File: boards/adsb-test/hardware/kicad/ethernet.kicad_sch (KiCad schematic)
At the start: 0 parts

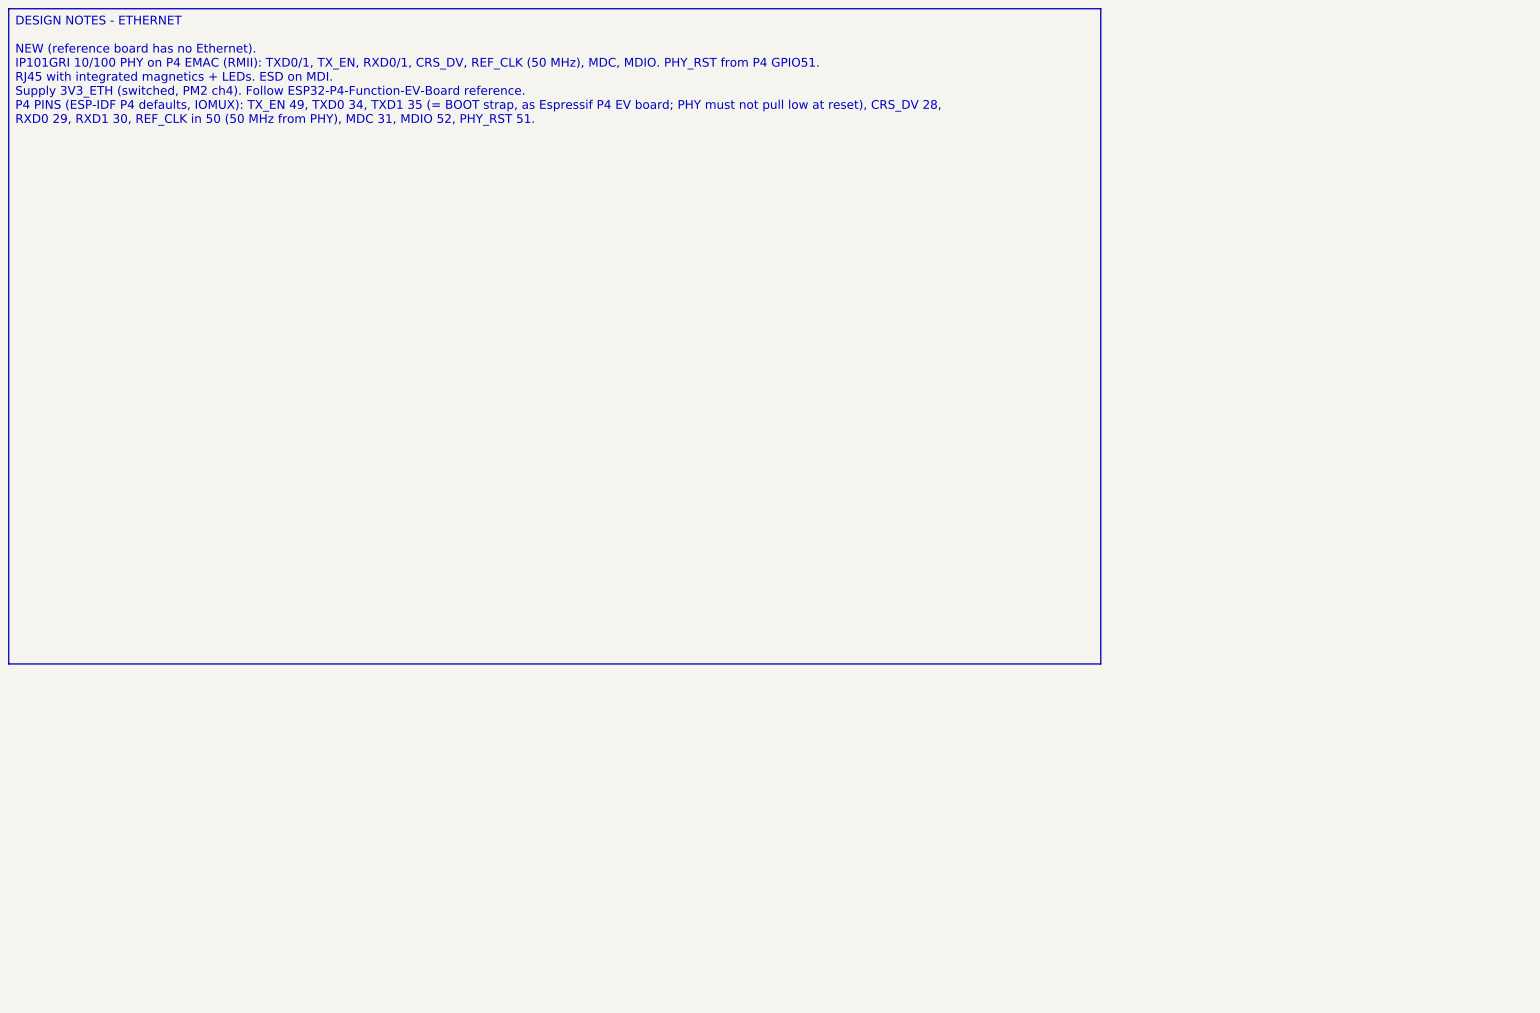
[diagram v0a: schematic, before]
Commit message: Release v0.22.0: all ADSB_Test schematic sheets generated (ERC clean)
Co-Authored-By: Claude Opus 5.5 <noreply@anthropic.com>
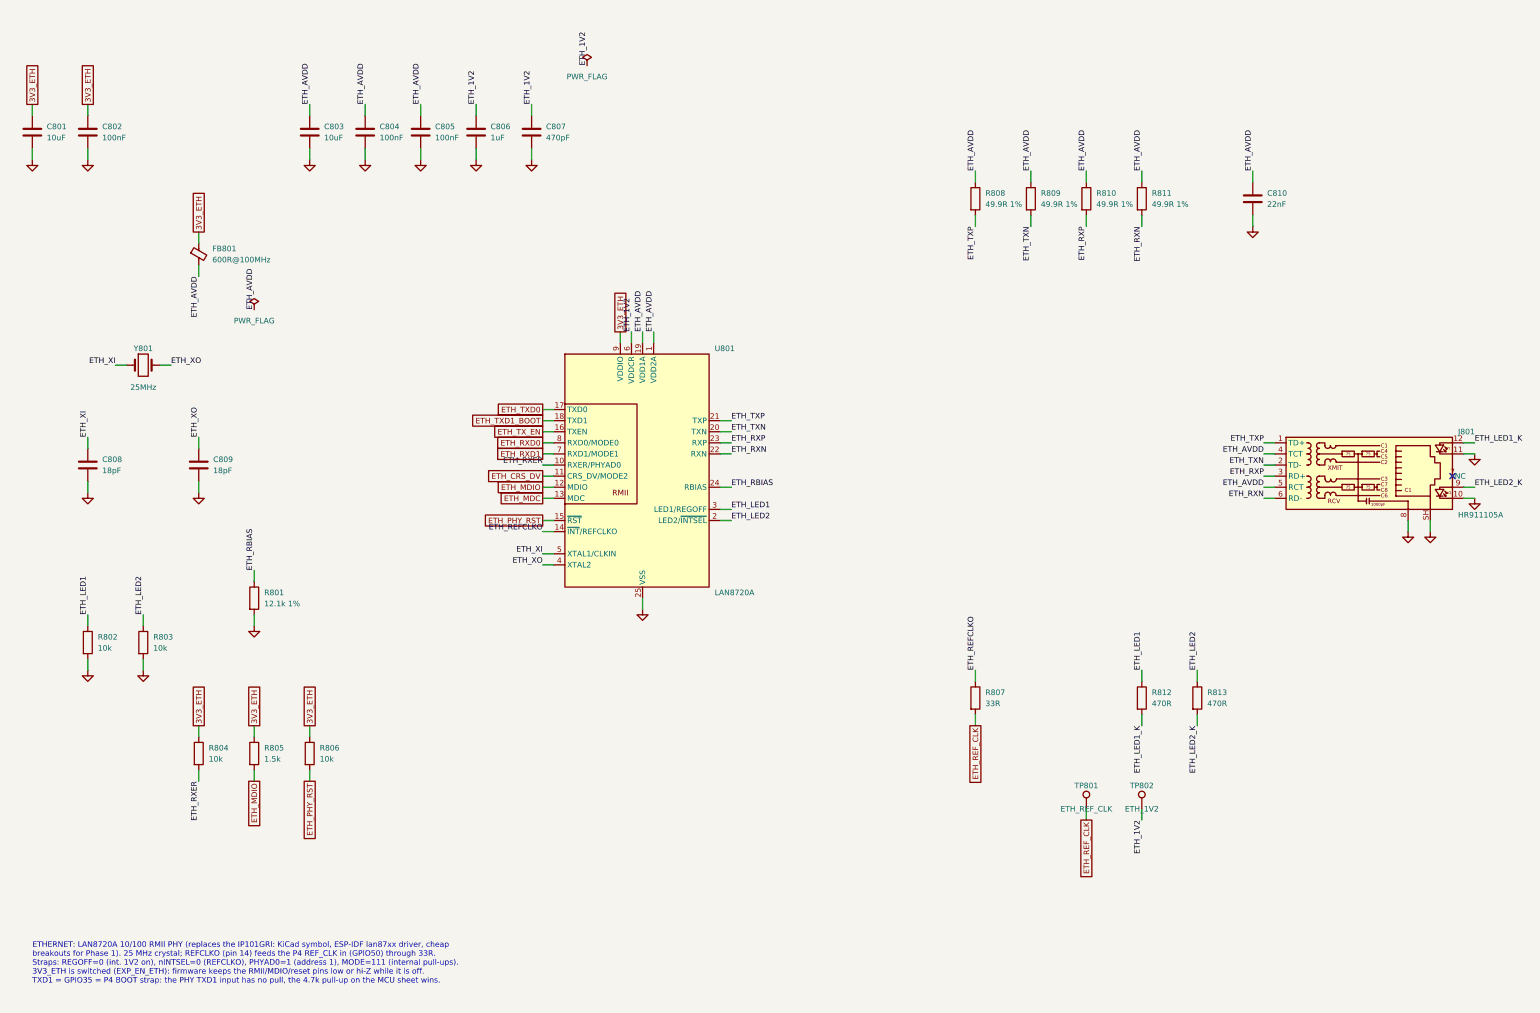
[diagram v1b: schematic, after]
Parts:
- added C801, C803: 10uF, Capacitor_SMD:C_1206_3216Metric_Pad1.33x1.80mm_HandSolder, symbol Device:C
- added C802, C804, C805: 100nF, Capacitor_SMD:C_0805_2012Metric_Pad1.18x1.45mm_HandSolder, symbol Device:C
- added C806: 1uF, Capacitor_SMD:C_0805_2012Metric_Pad1.18x1.45mm_HandSolder, symbol Device:C
- added C807: 470pF, Capacitor_SMD:C_0805_2012Metric_Pad1.18x1.45mm_HandSolder, symbol Device:C
- added C808, C809: 18pF, Capacitor_SMD:C_0805_2012Metric_Pad1.18x1.45mm_HandSolder, symbol Device:C
- added C810: 22nF, Capacitor_SMD:C_0805_2012Metric_Pad1.18x1.45mm_HandSolder, symbol Device:C
- added FB801: 600R@100MHz, Inductor_SMD:L_0805_2012Metric_Pad1.05x1.20mm_HandSolder, symbol Device:FerriteBead_Small
- added J801: HR911105A, Connector_RJ:RJ45_Hanrun_HR911105A_Horizontal, symbol Connector:RJ45_Hanrun_HR911105A_Horizontal
- added R801: 12.1k 1%, Resistor_SMD:R_0805_2012Metric_Pad1.20x1.40mm_HandSolder, symbol Device:R
- added R802, R803, R804, R806: 10k, Resistor_SMD:R_0805_2012Metric_Pad1.20x1.40mm_HandSolder, symbol Device:R
- added R805: 1.5k, Resistor_SMD:R_0805_2012Metric_Pad1.20x1.40mm_HandSolder, symbol Device:R
- added R807: 33R, Resistor_SMD:R_0805_2012Metric_Pad1.20x1.40mm_HandSolder, symbol Device:R
- added R808, R809, R810, R811: 49.9R 1%, Resistor_SMD:R_0805_2012Metric_Pad1.20x1.40mm_HandSolder, symbol Device:R
- added R812, R813: 470R, Resistor_SMD:R_0805_2012Metric_Pad1.20x1.40mm_HandSolder, symbol Device:R
- added TP801: ETH_REF_CLK, TestPoint:TestPoint_Pad_D1.5mm, symbol Connector:TestPoint
- added TP802: ETH_1V2, TestPoint:TestPoint_Pad_D1.5mm, symbol Connector:TestPoint
- added U801: LAN8720A, ADSB_Test:VQFN-24-1EP_4x4mm_P0.5mm_EP2.5x2.5mm_HandSolder, symbol Interface_Ethernet:LAN8720A
- added Y801: 25MHz, Crystal:Crystal_SMD_5032-2Pin_5.0x3.2mm_HandSoldering, symbol Device:Crystal
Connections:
- new net 3V3_ETH: C801.1, C802.1, FB801.1, R804.1, R805.1, R806.1, U801.9 (VDDIO)
- new net ETH_1V2: C806.1, C807.1, TP802.1, U801.6 (VDDCR)
- new net ETH_AVDD: C803.1, C804.1, C805.1, C810.1, FB801.2, J801.4 (TCT), J801.5 (RCT), R808.1, R809.1, R810.1, R811.1, U801.1 (VDD2A), U801.19 (VDD1A)
- new net ETH_CRS_DV: U801.11 (CRS_DV/MODE2)
- new net ETH_LED1: R802.1, R812.1, U801.3 (LED1/REGOFF)
- new net ETH_LED1_K: J801.12, R812.2
- new net ETH_LED2: R803.1, R813.1, U801.2 (LED2/~{INTSEL})
- new net ETH_LED2_K: J801.9, R813.2
- new net ETH_MDC: U801.13 (MDC)
- new net ETH_MDIO: R805.2, U801.12 (MDIO)
- new net ETH_PHY_RST: R806.2, U801.15 (~{RST})
- new net ETH_RBIAS: R801.1, U801.24 (RBIAS)
- new net ETH_REFCLKO: R807.1, U801.14 (~{INT}/REFCLKO)
- new net ETH_REF_CLK: R807.2, TP801.1
- new net ETH_RXD0: U801.8 (RXD0/MODE0)
- new net ETH_RXD1: U801.7 (RXD1/MODE1)
- new net ETH_RXER: R804.2, U801.10 (RXER/PHYAD0)
- new net ETH_RXN: J801.6 (RD-), R811.2, U801.22 (RXN)
- new net ETH_RXP: J801.3 (RD+), R810.2, U801.23 (RXP)
- new net ETH_TXD0: U801.17 (TXD0)
- new net ETH_TXD1_BOOT: U801.18 (TXD1)
- new net ETH_TXN: J801.2 (TD-), R809.2, U801.20 (TXN)
- new net ETH_TXP: J801.1 (TD+), R808.2, U801.21 (TXP)
- new net ETH_TX_EN: U801.16 (TXEN)
- new net ETH_XI: C808.1, U801.5 (XTAL1/CLKIN), Y801.1
- new net ETH_XO: C809.1, U801.4 (XTAL2), Y801.2
- new net GND: C801.2, C802.2, C803.2, C804.2, C805.2, C806.2, C807.2, C808.2, C809.2, C810.2, J801.10, J801.11, J801.8, J801.SH, R801.2, R802.2, R803.2, U801.25 (VSS)
- no-connect marks 0 -> 1
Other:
- note added: "ETHERNET: LAN8720A 10/100 RMII PHY (replaces the IP101GRI: KiCad symbol, ESP-IDF lan87xx driver, cheap breakouts for Phase 1). 25 MHz crystal; REFCLKO (pin 14) feeds the P4 REF_CLK in (GPIO50) through 33R. Straps: REGOFF=0 (int. 1V2 on), nINTSEL=0 (REFCLKO), PHYAD0=1 (address 1), MODE=111 (internal pull-ups). 3V3_ETH is switched (EXP_EN_ETH): firmware keeps the RMII/MDIO/reset pins low or hi-Z wh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"

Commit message: Release v0.22.1: LAN8720A strap pull-ups, microSD detect polarity, hand-saved datasheets
Co-Authored-By: Claude Opus 5.5 <noreply@anthropic.com>
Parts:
- added R814, R815, R816: 10k, Resistor_SMD:R_0805_2012Metric_Pad1.20x1.40mm_HandSolder, symbol Device:R
- R812, R813: value 470R -> 270R
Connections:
- net 3V3_ETH: now also R814.1, R815.1, R816.1
- net ETH_CRS_DV: now also R816.2
- net ETH_RXD0: now also R814.2
- net ETH_RXD1: now also R815.2
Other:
- note added: "ETHERNET: LAN8720A 10/100 RMII PHY (replaces the IP101GRI: KiCad symbol, ESP-IDF lan87xx driver, cheap breakouts for Phase 1). 25 MHz crystal; REFCLKO (pin 14) feeds the P4 REF_CLK in (GPIO50) through 33R. Straps: REGOFF=0 (int. 1V2 on), nINTSEL=0 (REFCLKO, 10k pull-down), PHYAD0=1 (address 1), MODE=111 (10k pull-ups: the P4 pins load the straps). LEDs active high via 270R. DS00002165: REFCLKO-mo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"
- note removed: "ETHERNET: LAN8720A 10/100 RMII PHY (replaces the IP101GRI: KiCad symbol, ESP-IDF lan87xx driver, cheap breakouts for Phase 1). 25 MHz crystal; REFCLKO (pin 14) feeds the P4 REF_CLK in (GPIO50) through 33R. Straps: REGOFF=0 (int. 1V2 on), nINTSEL=0 (REFCLKO), PHYAD0=1 (address 1), MODE=111 (internal pull-ups). 3V3_ETH is switched (EXP_EN_ETH): firmware keeps the RMII/MDIO/reset pins low or hi-Z wh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"

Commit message: Release v0.23.0: ADSB_Test BOM with DigiKey/LCSC codes and order links; 27 pF crystal load caps
Co-Authored-By: Claude Opus 5.5 <noreply@anthropic.com>
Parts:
- C808, C809: value 18pF -> 27pF
